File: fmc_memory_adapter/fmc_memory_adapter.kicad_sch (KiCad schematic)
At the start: 28 parts, among them J1 Gnd_Connector, J10 Lvl_Shifter_Address_Lines_8_15, J11 Lvl_Shifter_Address_Lines_0_7, J12 Conn_02x01, J14 Conn_02x03_Counter_Clockwise, J2 Conn_02x01, J3 Conn_02x01, J4 Conn_02x01, J5 Conn_02x01, J6 Lvl_Shifter_CE_OE_WE_UB_LB_ZZ, J7 Lvl_Shifter_Datalines_0_7, J8 Lvl_Shifter_Address_Lines_15_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, J9 Lvl_Shifter_Datalines_8_15, P0 ASP-134488-02, P1 CONN_02X32_DISCO1_LEFT_BACK, P2 CONN_02X32_DISCO1_RIGHT_BACK

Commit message: Add do not place markers to schematics
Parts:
- J12: value Conn_02x01 -> GND_Jumper5
- J14: value Conn_02x03_Counter_Clockwise -> Voltages_Connector
- J2: value Conn_02x01 -> GND_Jumper2
- J3: value Conn_02x01 -> GND_Jumper3
- J4: value Conn_02x01 -> GND_Jumper1
- J5: value Conn_02x01 -> GND_Jumper4
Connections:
- net at C1.2, C10.1, C11.1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: now also J1.12 (Pin_12); no longer J1.11 (Pin_11)
- no-connect marks 0 -> 429

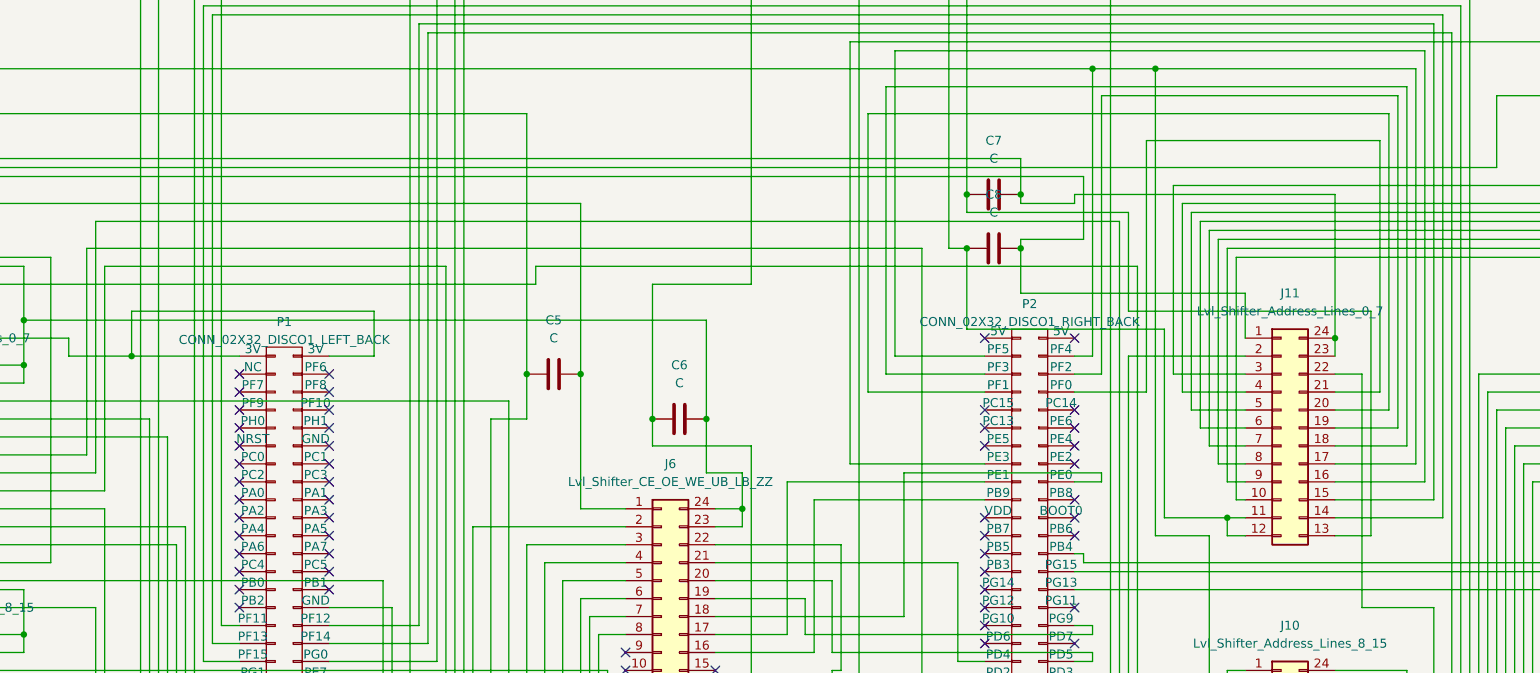
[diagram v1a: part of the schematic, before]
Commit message: Update schematics and footprints
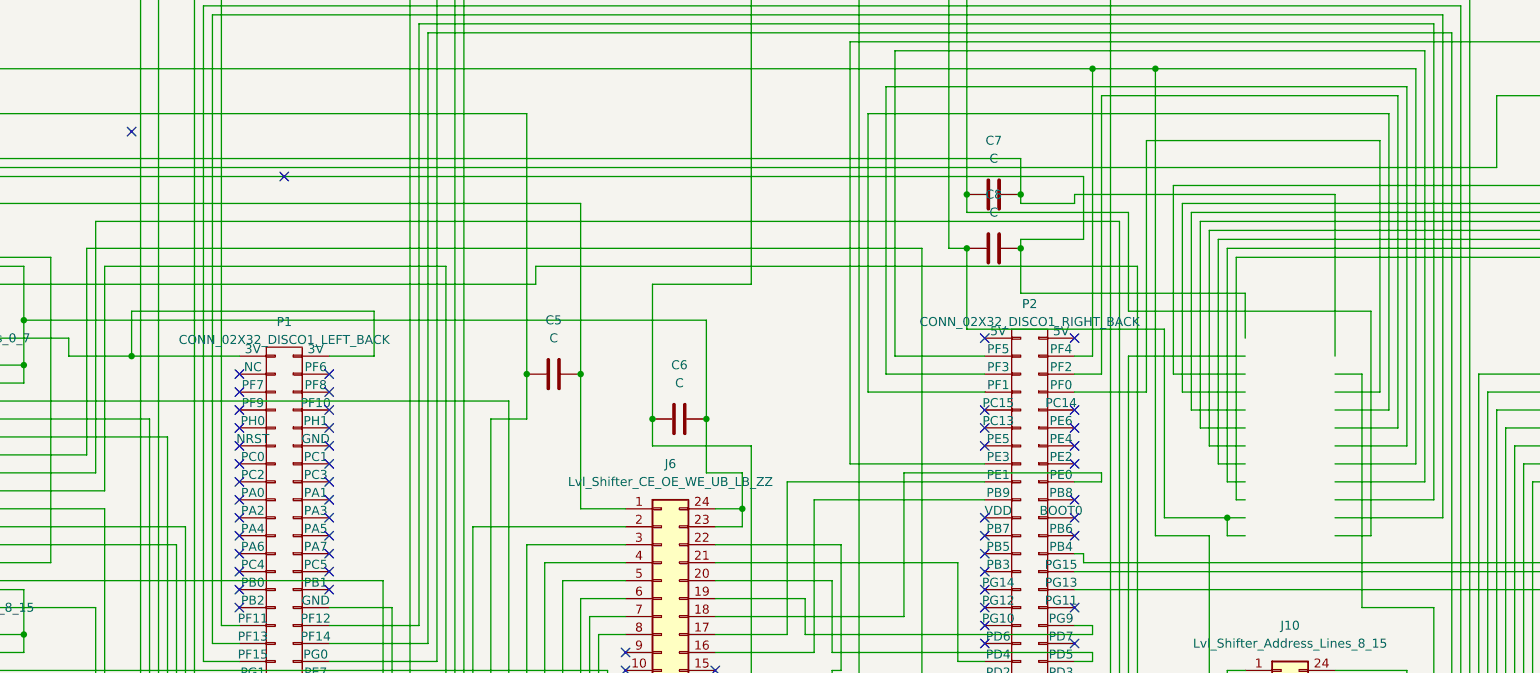
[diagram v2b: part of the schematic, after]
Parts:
- removed J11: Lvl_Shifter_Address_Lines_0_7, symbol Connector_Generic:Conn_02x12_Counter_Clockwise
- J1: footprint (none) -> Connector_PinHeader_2.54mm:PinHeader_2x08_P2.54mm_Vertical
- J12, J2, J3, J4, J5: footprint (none) -> Connector_PinHeader_2.54mm:PinHeader_1x02_P2.54mm_Vertical
- J14: footprint (none) -> Connector_PinHeader_2.54mm:PinHeader_2x03_P2.54mm_Vertical
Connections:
- no-connect marks 429 -> 431
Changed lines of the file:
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@@
 	)
 	(junction
-		(at 438.15 123.19)
-		(diameter 0)
-		(color 0 0 0 0)
-	)
-	(junction
 		(at 170.18 162.56)
 		(diameter 0)
@@
 	)
 	(no_connect
+		(at 289.56 100.33)
+	)
+	(no_connect
 		(at 412.75 254)
 	)
@@
 	)
 	(no_connect
+		(at 267.97 93.98)
+	)
+	(no_connect
 		(at 463.55 254)
 	)
@@
 	(wire
 		(pts
-			(xy 438.15 102.87) (xy 438.15 123.19)
-		)
-		(stroke
-			(width 0)
-			(type default)
-		)
-	)
-	(wire
-		(pts
 			(xy 232.41 152.4) (xy 232.41 154.94)
 		)
@@
 	(wire
 		(pts
-			(xy 438.15 123.19) (xy 438.15 125.73)
+			(xy 438.15 102.87) (xy 438.15 125.73)
 		)
 		(stroke
@@
 	)
 	(symbol
-		(lib_id "Connector_Generic:Conn_02x12_Counter_Clockwise")
-		(at 430.53 135.89 0)
-		(unit 1)
-		(exclude_from_sim no)
-		(in_bom yes)
-		(on_board yes)
-		(dnp no)
-		(fields_autoplaced yes)
-		(property "Reference" "J11"
-			(at 431.8 116.84 0)
-			(effects
-				(font
-					(size 1.27 1.27)
-				)
-			)
-		)
-		(property "Value" "Lvl_Shifter_Address_Lines_0_7"
-			(at 431.8 119.38 0)
-			(effects
-				(font
-					(size 1.27 1.27)
-				)
-			)
-		)
-		(property "Footprint" ""
-			(at 430.53 135.89 0)
-			(effects
-				(font
-					(size 1.27 1.27)
-				)
-				(hide yes)
-			)
-		)
-		(property "Datasheet" "~"
-			(at 430.53 135.89 0)
-			(effects
-				(font
-					(size 1.27 1.27)
-				)
-				(hide yes)
-			)
-		)
-		(property "Description" "Generic connector, double row, 02x12, counter clockwise pin numbering scheme (similar to DIP package numbering), script generated (kicad-library-utils/schlib/autogen/connector/)"
-			(at 430.53 135.89 0)
-			(effects
-				(font
-					(size 1.27 1.27)
-				)
-				(hide yes)
-			)
-		)
-		(pin "20"
-		)
-		(pin "24"
-		)
-		(pin "1"
-		)
-		(pin "12"
-		)
-		(pin "11"
-		)
-		(pin "13"
-		)
-		(pin "10"
-		)
-		(pin "4"
-		)
-		(pin "7"
-		)
-		(pin "8"
-		)
-		(pin "9"
-		)
-		(pin "5"
-		)
-		(pin "14"
-		)
-		(pin "19"
-		)
-		(pin "18"
-		)
-		(pin "21"
-		)
-		(pin "3"
-		)
-		(pin "22"
-		)
-		(pin "17"
-		)
-		(pin "16"
-		)
-		(pin "2"
-		)
-		(pin "23"
-		)
-		(pin "15"
-		)
-		(pin "6"
-		)
-		(instances
-			(project "FMC_Adaper"
-				(path "/87c78429-be2b-40ed-8d3b-56cb9666a56f"
-					(reference "J11")
-					(unit 1)
-				)
-			)
-		)
-	)
-	(symbol
 		(lib_id "Connector_Generic:Conn_02x01")
 		(at 124.46 86.36 0)
@@
 			)
 		)
-		(property "Footprint" ""
+		(property "Footprint" "Connector_PinHeader_2.54mm:PinHeader_1x02_P2.54mm_Vertical"
 			(at 124.46 86.36 0)
 			(effects
@@
 			)
 		)
-		(property "Footprint" ""
+		(property "Footprint" "Connector_PinHeader_2.54mm:PinHeader_1x02_P2.54mm_Vertical"
 			(at 124.46 90.17 0)
 			(effects
@@
 			)
 		)
-		(property "Footprint" ""
+		(property "Footprint" "Connector_PinHeader_2.54mm:PinHeader_2x08_P2.54mm_Vertical"
 			(at 147.32 90.17 0)
 			(effects
@@
 			)
 		)
-		(property "Footprint" ""
+		(property "Footprint" "Connector_PinHeader_2.54mm:PinHeader_1x02_P2.54mm_Vertical"
 			(at 124.46 97.79 0)
 			(effects
@@
 			)
 		)
-		(property "Footprint" ""
+		(property "Footprint" "Connector_PinHeader_2.54mm:PinHeader_2x03_P2.54mm_Vertical"
 			(at 147.32 113.03 0)
 			(effects
@@
 			)
 		)
-		(property "Footprint" ""
+		(property "Footprint" "Connector_PinHeader_2.54mm:PinHeader_1x02_P2.54mm_Vertical"
 			(at 124.46 93.98 0)
 			(effects
@@
 			)
 		)
-		(property "Footprint" ""
+		(property "Footprint" "Connector_PinHeader_2.54mm:PinHeader_1x02_P2.54mm_Vertical"
 			(at 124.46 82.55 0)
 			(effects

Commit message: Update Schematic
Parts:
- removed C1, C10, C11, C12, C2, C3, C4, C5, C6, C7, C8, C9: C, symbol Device:C
- removed J1: Gnd_Connector, Connector_PinHeader_2.54mm:PinHeader_2x08_P2.54mm_Vertical, symbol Connector_Generic:Conn_02x07_Counter_Clockwise
- removed J10: Lvl_Shifter_Address_Lines_8_15, symbol Connector_Generic:Conn_02x12_Counter_Clockwise
- removed J14: Voltages_Connector, Connector_PinHeader_2.54mm:PinHeader_2x03_P2.54mm_Vertical, symbol Connector_Generic:Conn_02x03_Counter_Clockwise
- removed J6: Lvl_Shifter_CE_OE_WE_UB_LB_ZZ, symbol Connector_Generic:Conn_02x12_Counter_Clockwise
- removed J7: Lvl_Shifter_Datalines_0_7, symbol Connector_Generic:Conn_02x12_Counter_Clockwise
- removed J8: Lvl_Shifter_Address_Lines_15_23, symbol Connector_Generic:Conn_02x12_Counter_Clockwise
- removed J9: Lvl_Shifter_Datalines_8_15, symbol Connector_Generic:Conn_02x12_Counter_Clockwise
- added C1, C10, C11, C12, C2, C3, C4, C5, C6, C7, C8, C9: C0805C104K5RAC7411, custom_footprints:CAPC2012X88N, symbol C0805C104K5RAC7411:C0805C104K5RAC7411
- added IC1, IC2, IC3, IC4, IC5, IC6: SN74AVC8T245PWG4, custom_footprints:SOP65P640X120-24N, symbol SN74AVC8T245PWG4:SN74AVC8T245PWG4
- added J1: Conn_02x07_Odd_Even, Connector_PinHeader_2.54mm:PinHeader_2x07_P2.54mm_Vertical, symbol Connector_Generic:Conn_02x07_Odd_Even
- added J6: Conn_02x03_Odd_Even, Connector_PinHeader_2.54mm:PinHeader_2x03_P2.54mm_Vertical, symbol Connector_Generic:Conn_02x03_Odd_Even
- J0: renamed from P0; footprint SAMTEC_FMC:SAMTEC_ASP-134488-02 -> custom_footprints:ASP13448802; Datasheet_1 http://suddendocs.samtec.com/prints/asp-134488-02-mkt.pdf -> (none); Footprint_1 ASP13448802 -> (none); Reference_1 J -> (none); Value_1 ASP-134488-02 -> (none)
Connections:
- net at J2.2 (Pin_2): now also J1.3 (Pin_3)
- net at J3.2 (Pin_2): now also J1.5 (Pin_5)
- net at J4.2 (Pin_2): now also J1.1 (Pin_1)
- net at P2.4 (PF4), P2.63 (GND), P2.64 (GND): now also IC2.17 (B5), J1.4 (Pin_4)
- net at P1.30 (GND), P1.63 (GND), P1.64 (GND): now also J1.2 (Pin_2)
- net at J5.2 (Pin_2): now also J1.7 (Pin_7)
- net at J12.2 (Pin_2): now also J1.11 (Pin_11), J1.13 (Pin_13), J1.9 (Pin_9)
- net at J0.C10: now also IC5.3 (A1)
- net at J0.C11: now also IC5.4 (A2)
- net at J0.C14: now also IC5.5 (A3)
- net at J0.C15: now also IC5.6 (A4)
- net at J0.C18: now also IC5.7 (A5)
- net at J0.C19: now also IC5.8 (A6)
- net at J0.C22: now also IC5.9 (A7)
- net at J0.C23: now also IC5.10 (A8)
- net at J0.C26: now also IC6.3 (A1)
- net at J0.C27: now also IC6.4 (A2)
- net at J0.C39: now also J6.5 (Pin_5)
- net at J0.D11: now also IC6.7 (A5)
- net at J0.D12: now also IC6.8 (A6)
- net at J0.D14: now also IC6.9 (A7)
- net at J0.D15: now also IC6.10 (A8)
- net at J0.D17: now also IC2.3 (A1)
- net at J0.D18: now also IC2.4 (A2)
- net at J0.D20: now also IC2.5 (A3)
- net at J0.D21: now also IC2.6 (A4)
- net at J0.D23: now also IC2.7 (A5)
- net at J0.D24: now also IC2.8 (A6)
- net at J0.D26: now also IC2.9 (A7)
- net at J0.D27: now also IC2.10 (A8)
- net at J0.D36: now also J6.3 (Pin_3)
- net at J0.D8: now also C1.2, C10.1, C11.1, C12.1, C2.2, C3.1, C4.1, C5.1, C6.1, C7.1, C8.1, C9.1, IC1.11 (GND_1), IC1.12 (GND_2), IC1.13 (GND_3), IC2.11 (GND_1), IC2.12 (GND_2), IC2.13 (GND_3), IC3.11 (GND_1), IC3.12 (GND_2), IC3.13 (GND_3), IC4.11 (GND_1), IC4.12 (GND_2), IC4.13 (GND_3), IC5.11 (GND_1), IC5.12 (GND_2), IC5.13 (GND_3), IC6.11 (GND_1), IC6.12 (GND_2), IC6.5 (A3), J1.6 (Pin_6)
- net at J0.D9: now also IC6.6 (A4)
- net at J0.G10: now also IC1.6 (A4)
- net at J0.G12: now also IC1.7 (A5)
- net at J0.G13: now also IC1.8 (A6)
- net at J0.G15: now also IC1.9 (A7)
- net at J0.G16: now also IC1.10 (A8)
- net at J0.G18: now also IC3.3 (A1)
- net at J0.G19: now also IC3.4 (A2)
- net at J0.G21: now also IC3.5 (A3)
- net at J0.G22: now also IC3.6 (A4)
- net at J0.G24: now also IC3.7 (A5)
- net at J0.G25: now also IC3.8 (A6)
- net at J0.G27: now also IC3.9 (A7)
- net at J0.G28: now also IC3.10 (A8)
- net at J0.G30: now also IC4.3 (A1)
- net at J0.G31: now also IC4.4 (A2)
- net at J0.G33: now also IC4.5 (A3)
- net at J0.G34: now also IC4.6 (A4)
- net at J0.G36: now also IC4.7 (A5)
- net at J0.G37: now also IC4.8 (A6)
- net at J0.G6: now also IC1.3 (A1)
- net at J0.G7: now also IC1.4 (A2)
- net at J0.G9: now also IC1.5 (A3)
- net at J0.H10: now also IC1.2 (DIR), IC2.2 (DIR), IC3.2 (DIR), IC4.2 (DIR)
- net at J0.H11: now also J6.1 (Pin_1)
- net at J0.H7: now also IC1.22 (~{OE}), IC2.22 (~{OE}), IC3.22 (~{OE}), IC4.22 (~{OE}), IC5.22 (~{OE}), IC6.22 (~{OE})
- net at J0.H8: now also IC5.2 (DIR), IC6.2 (DIR)
- net at P1.41 (PE10): now also IC5.14 (B8)
- net at P1.40 (PE9): now also IC5.15 (B7)
- net at P1.39 (PE8): now also IC5.16 (B6)
- net at P1.38 (PE7): now also IC5.17 (B5)
- net at P2.42 (PD1): now also IC5.18 (B4)
- net at P2.41 (PD0): now also IC5.19 (B3)
- net at P1.60 (PD15): now also IC5.20 (B2)
- net at P1.59 (PD14): now also IC5.21 (B1)
- net at P1.1 (3V), P1.2 (3V): now also J6.6 (Pin_6)
- net at P1.31 (PF11): now also IC3.17 (B5)
- net at P1.32 (PF12): now also IC2.15 (B7)
- net at P1.33 (PF13): now also IC2.14 (B8)
- net at P1.34 (PF14): now also IC1.21 (B1)
- net at P1.35 (PF15): now also IC1.20 (B2)
- net at P1.36 (PG0): now also IC1.19 (B3)
- net at P1.37 (PG1): now also IC1.18 (B4)
- net at P1.42 (PE11): now also IC6.21 (B1)
- net at P1.43 (PE12): now also IC6.13 (GND_3), IC6.20 (B2)
- net at P1.44 (PE13): now also IC6.19 (B3)
- net at P1.45 (PE14): now also IC6.18 (B4)
- net at P1.46 (PE15): now also IC6.17 (B5)
- net at P1.53 (PD8): now also IC6.16 (B6)
- net at P1.54 (PD9): now also IC6.15 (B7)
- net at P1.55 (PD10): now also IC6.14 (B8)
- net at P1.56 (PD11): now also IC3.21 (B1)
- net at P1.57 (PD12): now also IC3.20 (B2)
- net at P1.58 (PD13): now also IC3.19 (B3)
- net at P1.61 (PG2): now also IC1.17 (B5)
- net at P1.62 (PG3): now also IC1.16 (B6)
- net at P2.62 (PG5): now also IC1.14 (B8)
- net at P2.61 (PG4): now also IC1.15 (B7)
- net at P2.19 (PB9): now also IC4.16 (B6)
- net at P2.17 (PE1): now also IC4.17 (B5)
- net at P2.18 (PE0): now also IC4.18 (B4)
- net at P2.34 (PG9): now also IC4.19 (B3)
- net at P2.38 (PD5): now also IC4.20 (B2)
- net at P2.37 (PD4): now also IC4.21 (B1)
- net at P2.15 (PE3): now also IC3.18 (B4)
- net at P2.26 (PB4): now also IC3.14 (B8)
- net at P2.28 (PG15): now also IC3.15 (B7)
- net at P2.3 (PF5): now also IC2.16 (B6)
- net at P2.30 (PG13): now also IC3.16 (B6)
- net at P2.5 (PF3): now also IC2.18 (B4)
- net at P2.6 (PF2): now also IC2.19 (B3)
- net at P2.7 (PF1): now also IC2.20 (B2)
- net at P2.8 (PF0): now also IC2.21 (B1)
- new net: C1.1, C10.2, C11.2, C6.2, C7.2, IC1.23 (VCCB_1), IC1.24 (VCCB_2), IC2.23 (VCCB_1), IC2.24 (VCCB_2), IC3.23 (VCCB_1), IC3.24 (VCCB_2), IC4.23 (VCCB_1), IC4.24 (VCCB_2), IC5.23 (VCCB_1), IC5.24 (VCCB_2), J6.4 (Pin_4)
- new net: C12.2, C2.1, C3.2, C4.2, C5.2, C8.2, C9.2, IC1.1 (VCCA), IC2.1 (VCCA), IC3.1 (VCCA), IC4.1 (VCCA), IC5.1 (VCCA), IC6.1 (VCCA), IC6.23 (VCCB_1), IC6.24 (VCCB_2), J6.2 (Pin_2)
- no-connect marks 431 -> 429

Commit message: Add schematics and fmc controller
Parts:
- removed C10, C4: C0805C104K5RAC7411, custom_footprints:CAPC2012X88N, symbol C0805C104K5RAC7411:C0805C104K5RAC7411
- removed J1: Conn_02x07_Odd_Even, Connector_PinHeader_2.54mm:PinHeader_2x07_P2.54mm_Vertical, symbol Connector_Generic:Conn_02x07_Odd_Even
- added C1, C11: C0805C104K5RAC7411, custom_footprints:CAPC2012X88N, symbol C0805C104K5RAC7411:C0805C104K5RAC7411
- added H1, H2, H3, H4, H5, H6, H7, H8, H9: MountingHole, MountingHole:MountingHole_2.2mm_M2_Pad_TopBottom, symbol Mechanical:MountingHole
- added J10: Conn_02x08_Odd_Even, Connector_PinHeader_2.54mm:PinHeader_2x08_P2.54mm_Vertical, symbol Connector_Generic:Conn_02x08_Odd_Even
- added J9: Conn_01x03, Connector_PinHeader_2.54mm:PinHeader_1x03_P2.54mm_Vertical, symbol Connector_Generic:Conn_01x03
- renumbered C11 to C10, C1 to C4, IC5 to IC1, IC6 to IC2, IC4 to IC3, IC2 to IC4, IC1 to IC5, IC3 to IC6, J4 to J1, J5 to J4, J12 to J5, J6 to J7, J0 to J8
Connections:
- net at C5.1, C8.1, C9.1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: now also C3.2, C1.1, C11.1, J10.6 (Pin_6); no longer C10.1, C12.1, C2.2, C3.1, C4.2, C6.1, C7.1, IC1.13 (GND_3), IC2.5 (A3), IC3.13 (GND_3), IC4.13 (GND_3), IC5.13 (GND_3), IC6.13 (GND_3), J8.D8
- net at C10.2, C4.1, C6.2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: now also C12.2, C2.2, IC2.23 (VCCB_1), IC2.24 (VCCB_2)
- net at C5.2, C8.2, C9.2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: now also C3.1, C1.2, C11.2; no longer C12.2, C2.1, C3.2, IC2.23 (VCCB_1), IC2.24 (VCCB_2)
- net at IC3.2 (DIR), IC4.2 (DIR), IC5.2 (DIR)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: now also J9.2 (Pin_2)
- net at IC1.22 (~{OE}), IC2.22 (~{OE}), IC3.22 (~{OE})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: now also J9.1 (Pin_1)
- net at J2.2 (Pin_2): now also J10.3 (Pin_3)
- net at J3.2 (Pin_2): now also J10.5 (Pin_5)
- net at IC1.2 (DIR), IC2.2 (DIR), J8.H8: now also J9.3 (Pin_3)
- net at J8.C26: now also IC2.4 (A2); no longer IC2.3 (A1)
- net at J8.C27: now also IC2.3 (A1); no longer IC2.4 (A2)
- net at J5.2 (Pin_2): now also J10.11 (Pin_11), J10.13 (Pin_13), J10.9 (Pin_9)
- net at P1.30 (GND), P1.63 (GND), P1.64 (GND): now also J10.2 (Pin_2)
- net at IC2.20 (B2), P1.43 (PE12): no longer IC2.13 (GND_3)
- net at J4.2 (Pin_2): now also J10.7 (Pin_7)
- net at P2.63 (GND), P2.64 (GND): now also J10.4 (Pin_4); no longer IC4.17 (B5), P2.4 (PF4)
- net at J1.2 (Pin_2): now also J10.1 (Pin_1)
- new net: C10.1, C12.1, C2.1, C4.2, C6.1, C7.1, IC1.13 (GND_3), IC2.13 (GND_3), IC3.13 (GND_3), IC4.13 (GND_3), IC5.13 (GND_3), IC6.13 (GND_3), J10.8 (Pin_8)
- new net: IC2.5 (A3), J8.D8
- new net: IC4.17 (B5), P2.4 (PF4)
- new net GND: J10.15 (Pin_15)
